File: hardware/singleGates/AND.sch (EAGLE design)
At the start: 13 parts

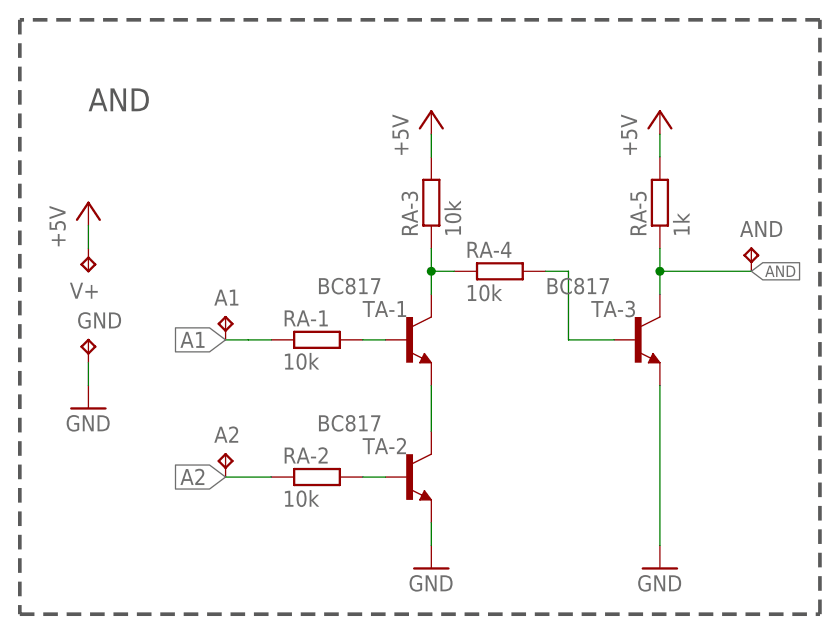
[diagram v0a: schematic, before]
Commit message: Board files are just confusing at the moment
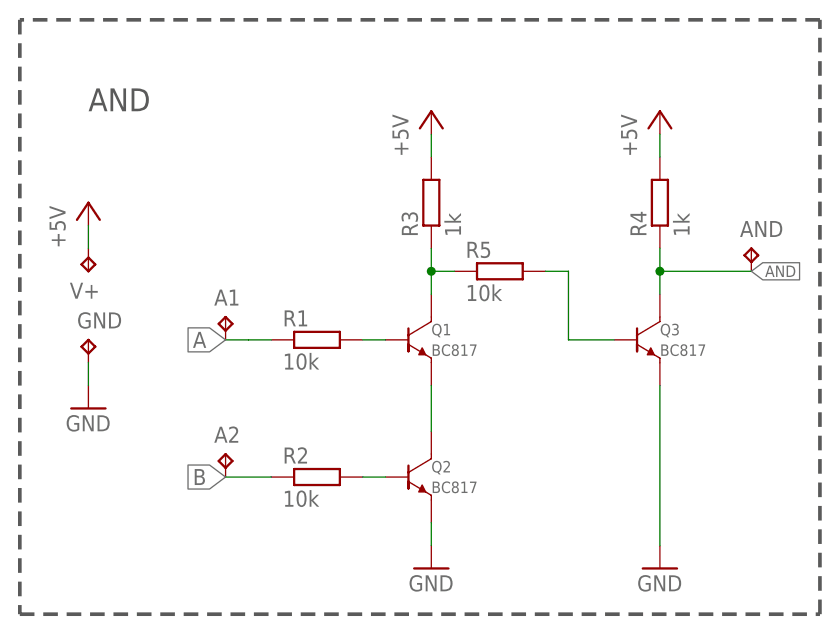
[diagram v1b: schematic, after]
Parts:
- removed RA-1, RA-2, RA-3, RA-4: 10k, p.peter-rcl:R-EU_R0603
- removed RA-5: 1k, p.peter-rcl:R-EU_R0603
- removed TA-1, TA-2, TA-3: BC817, transistor:BC817-40-NPN-SOT23-BEC
- added Q1, Q2, Q3: BC817, p.peter-scoville.tests:TRANSISTOR-NPN-GENERICDEFAULT-SOT23-BEC
- added R1, R2, R5: 10k, p.peter-scoville.tests:R-EU_R0603
- added R3, R4: 1k, p.peter-scoville.tests:R-EU_R0603
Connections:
- removed net A1: A1.TP, RA-1.1
- removed net A2: A2.TP, RA-2.1
- new net A: A1.TP, R1.1
- new net B: A2.TP, R2.1
- net +5V: now also R3.2, R4.2; no longer RA-3.2, RA-5.2
- net AND: now also Q3.COLLECTOR, R4.1; no longer RA-5.1, TA-3.C
- net GND: now also Q2.EMITTER, Q3.EMITTER; no longer TA-2.E, TA-3.E
- net N$1: now also Q1.BASE, R1.2; no longer RA-1.2, TA-1.B
- net N$15: now also Q3.BASE, R5.2; no longer RA-4.2, TA-3.B
- net N$2: now also Q1.COLLECTOR, R3.1, R5.1; no longer RA-3.1, RA-4.1, TA-1.C
- net N$3: now also Q2.BASE, R2.2; no longer RA-2.2, TA-2.B
- net N$4: now also Q1.EMITTER, Q2.COLLECTOR; no longer TA-1.E, TA-2.C
